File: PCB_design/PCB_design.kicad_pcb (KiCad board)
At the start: 2 copper layers, 59.7 x 59.7 mm, 48 parts, among them J10 Conn_01x01_Socket, J11 Conn_01x01_Socket, J2 Conn_01x04_Socket, J3 Conn_01x01_Socket, J4 Conn_01x02_Pin, J5 Conn_01x01_Socket, J6 Conn_01x01_Socket, J7 Conn_01x01_Socket, J8 Conn_01x01_Socket, J9 USB_C_Receptacle_PowerOnly_6P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

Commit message: Added PCB design pdf
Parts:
- moved C1 42.1 mm to (99.2, 42.2)
- moved C10 42.1 mm to (102.1, 79.0)
- moved C4 42.1 mm to (111.7, 74.7)
- moved C5 42.1 mm to (93.9, 69.4)
- moved C6 42.1 mm to (105.2, 41.3)
- moved C9 42.1 mm to (106.2, 86.6)
- moved D1 42.1 mm to (92.0, 39.6)
- moved D10 42.1 mm to (109.9, 84.9)
- moved D11 42.1 mm to (109.9, 83.3)
- moved D17 42.1 mm to (106.2, 44.2)
- moved D3 42.1 mm to (96.0, 39.5)
- moved J11 42.1 mm to (82.3, 65.2)
- moved J4 42.1 mm to (121.9, 67.9)
- moved Q1 42.1 mm to (99.2, 75.2)
- moved R5 42.1 mm to (105.8, 84.9)
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
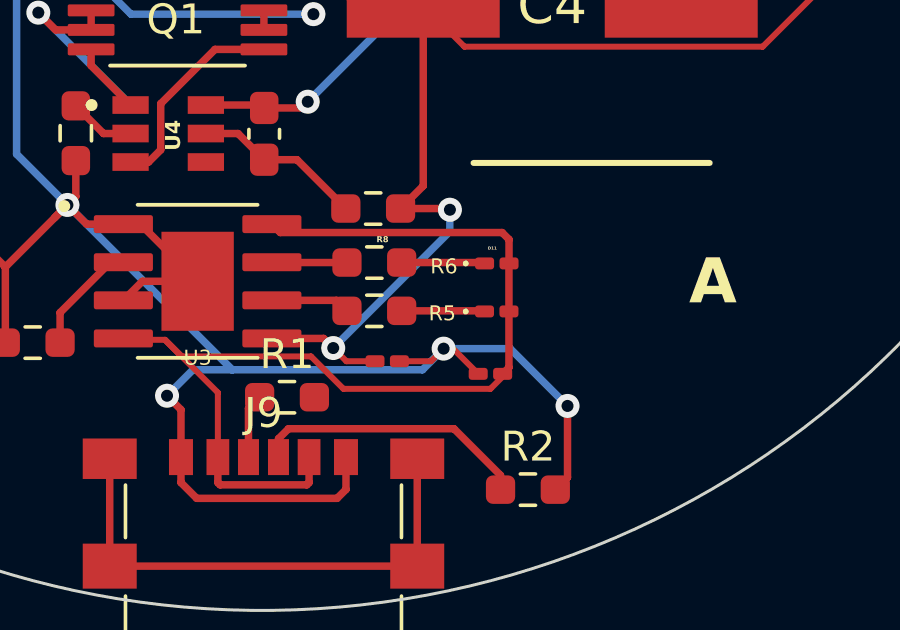
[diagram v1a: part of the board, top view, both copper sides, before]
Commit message: Added design for in parallel transducer plug in
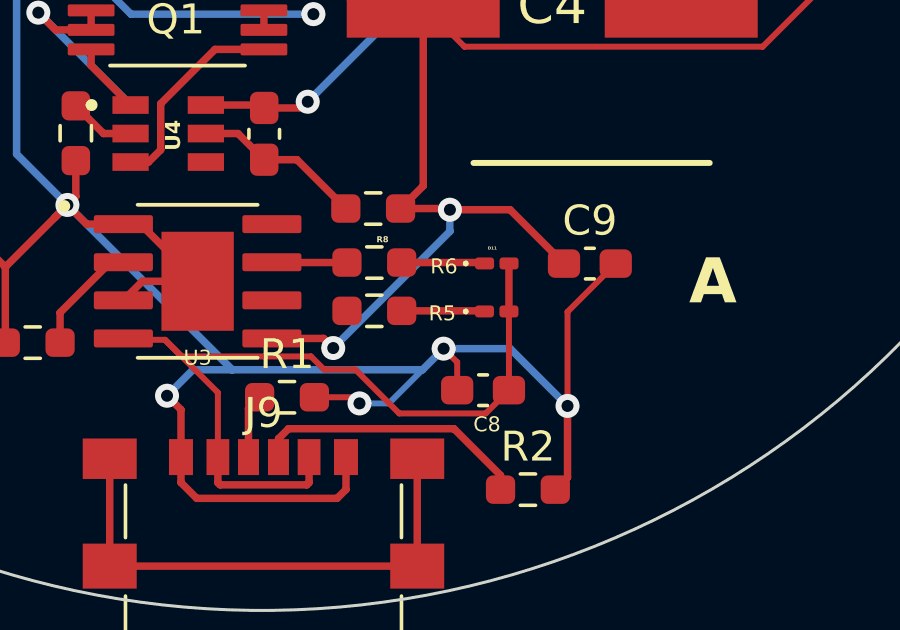
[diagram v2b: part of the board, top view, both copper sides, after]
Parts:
- C8, C9: footprint Capacitor_SMD:C_0201_0603Metric_Pad0.64x0.40mm_HandSolder -> Capacitor_SMD:C_0603_1608Metric_Pad1.08x0.95mm_HandSolder
- moved C9 7.50 mm to (113.0, 83.3)
- moved C8 0.60 mm to (109.4, 87.5)
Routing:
- net GND_Arduino1: track 245.9 -> 253.9 mm, vias 13 -> 14
- net Net-(D10-A): track 35.7 -> 27.9 mm
- net Bat+: track 54.1 -> 57.1 mm
- net Hold: track 2.65 -> 0.00 mm

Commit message: Add new PCB Design
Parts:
- removed Q1: FS8205A, FS8205A:SOP65P640X120-8N
- added Q2: FS8205, FS8205:SOT95P280X145-6N, F.Cu at (95.3, 82.9)
- added SW1: SW_SPDT, MINI-SPDT-SW:SW_MINI-SPDT-SW, F.Cu at (85.1, 83.3)
- C4: footprint Capacitor_220uF35V_smaller:CAPAE1050X1050N -> Capacitor_SMD:CP_Elec_6.3x7.7
- C5: footprint Capacitor_SMD:C_0201_0603Metric_Pad0.64x0.40mm_HandSolder -> Capacitor_SMD:C_0603_1608Metric_Pad1.08x0.95mm_HandSolder
- C7: footprint Capacitor_220uF35V_smaller:CAPAE1050X1050N -> CAP-SMD_BD10.0-L10.3-W10.3-FD:CAP-SMD_BD10.0-L10.3-W10.3-FD
- D1, D2, D3, D4, D5, D6, D7, D8: footprint Diode_SMD:D_0603_1608Metric_Pad1.05x0.95mm_HandSolder -> Diode_SMD:D_0805_2012Metric_Pad1.15x1.40mm_HandSolder
- L1: footprint Inductor_SMD:L_7.3x7.3_H3.5 -> Inductor_SMD:ND-SMD_L11.6-W10.1_final_13mm
- moved J4 41.7 mm to (82.8, 53.5), turned to 59 degrees
- moved D1 39.2 mm to (126.3, 58.7), turned to 90 degrees
- moved D2 36.6 mm to (126.3, 54.1), turned to 90 degrees
- moved C9 36.5 mm to (78.8, 70.6), turned to -90 degrees
- moved D3 35.8 mm to (121.6, 64.5)
- moved C1 35.1 mm to (113.0, 74.5), turned to 180 degrees
- moved C4 34.6 mm to (79.1, 63.2), turned to 180 degrees
- moved J11 34.3 mm to (103.4, 38.1), turned to 180 degrees
- moved J10 34.1 mm to (105.6, 38.1), turned to 180 degrees
- moved R9 34.1 mm to (117.1, 74.5)
- moved J8 33.7 mm to (119.3, 46.5), turned to 0 degrees
- moved D17 33.3 mm to (120.2, 74.5), turned to 180 degrees
- moved D4 33.1 mm to (121.6, 62.2)
- moved J2 33.0 mm to (110.3, 42.6), turned to 90 degrees
- moved C6 32.8 mm to (97.3, 73.1), turned to -90 degrees
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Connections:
- J4 pad 2: Bat+ -> Net-(J4-Pin_2)
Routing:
- net Net-(J4-Pin_2): track 0.00 -> 35.4 mm
- net Batt-: track 32.8 -> 47.5 mm, vias 2 -> 1
- net Bat+: track 57.1 -> 68.8 mm, vias 2 -> 0
- net Net-(D9-B): track 30.3 -> 41.0 mm
- net GND_Arduino1: track 253.9 -> 243.3 mm, vias 14 -> 16
- net OUT2: track 30.4 -> 20.0 mm
- net Boost_Out: track 87.9 -> 95.6 mm
- net +5V Arduino: track 53.8 -> 60.2 mm, vias 2 -> 1
- net Net-(Q1-Pad1): track 5.76 -> 0.00 mm
- net Net-(J9-CC2): track 9.27 -> 5.32 mm
- net OUT4: track 21.5 -> 25.3 mm
- net Net-(D17-A): track 5.02 -> 1.74 mm
- net A1: track 11.5 -> 14.2 mm
- net Net-(Q2-Pad2): track 0.00 -> 2.51 mm
- net Net-(U4-OD): track 2.40 -> 4.91 mm
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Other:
- board size 59.7 x 59.7 mm -> 60 x 60 mm
